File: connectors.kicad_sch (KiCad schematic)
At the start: 4 parts

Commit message: Schematic design complete
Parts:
- J1, J2: renamed from J?; footprint (none) -> Connector_PinHeader_2.54mm:PinHeader_1x04_P2.54mm_Vertical
- J3: renamed from J?; footprint (none) -> Connector_PinHeader_2.54mm:PinHeader_1x09_P2.54mm_Vertical
- J4: renamed from J?; footprint (none) -> Connector_PinHeader_2.54mm:PinHeader_2x03_P2.54mm_Vertical
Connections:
- net MISO: now reaches J4.1 (Pin_1)
- net Vcc: now reaches J4.2 (Pin_2)
- net Vcc: now also J1.2 (Pin_2), J2.2 (Pin_2), J3.9 (Pin_9)
- net SCK: now reaches J4.3 (Pin_3)
- net SCK: now also J1.4 (Pin_4)
- net MOSI: now reaches J4.4 (Pin_4)
- net RESET: now reaches J4.5 (Pin_5)
- net GND: now reaches J4.6 (Pin_6)
- net GND: now also J1.1 (Pin_1), J2.1 (Pin_1), J3.8 (Pin_8)
- net D2: now reaches J3.1 (Pin_1)
- net D3: now reaches J3.2 (Pin_2)
- net D4: now reaches J3.3 (Pin_3)
- net D5: now reaches J3.4 (Pin_4)
- net D6: now reaches J3.5 (Pin_5)
- net D7: now reaches J3.6 (Pin_6)
- net D8: now reaches J3.7 (Pin_7)
- net SDA: now reaches J1.3 (Pin_3)
- net RX: now reaches J2.3 (Pin_3)
- net TX: now reaches J2.4 (Pin_4)
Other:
- note added: "Connectors"
- title: (none) -> ${project_name}
- moved on the sheet: J1, J2, J3, J4
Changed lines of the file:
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@@
 (kicad_sch (version 20211123) (generator eeschema)
   (paper "A4")
-  (symbol (lib_id "Connector_Generic:Conn_02x03_Odd_Even") (at 222.25 112.395 0) (unit 1)
+  (title_block
+    (title "${project_name}")
+    (date "2022-08-29")
+    (rev "1")
+    (comment 1 "Project #2, KiCad Like a Pro Udemy course")
+    (comment 2 "MCU Datalogger with memory and clock")
+    (comment 3 "github.com/raghavmarwah")
+    (comment 4 "raghavmarwah.com")
+  )
+  (polyline (pts (xy 193.04 59.69) (xy 193.04 144.78))
+    (stroke (width 0) (type default) (color 0 0 0 0))
+  )
+  (polyline (pts (xy 92.075 59.69) (xy 92.075 60.325))
+    (stroke (width 0) (type default) (color 0 0 0 0))
+  )
+  (polyline (pts (xy 92.075 60.325) (xy 92.075 144.78))
+    (stroke (width 0) (type default) (color 0 0 0 0))
+  )
+  (polyline (pts (xy 92.075 144.78) (xy 193.04 144.78))
+    (stroke (width 0) (type default) (color 0 0 0 0))
+  )
+  (polyline (pts (xy 193.04 59.69) (xy 92.075 59.69))
+    (stroke (width 0) (type default) (color 0 0 0 0))
+  )
+  (text "Connectors" (at 92.075 59.69 0)
+    (effects (font (size 1.27 1.27)) (justify left bottom))
+  )
+  (hierarchical_label "Vcc" (shape passive) (at 125.095 81.915 0)
+    (effects (font (size 1.27 1.27)) (justify left))
+  )
+  (hierarchical_label "GND" (shape passive) (at 160.655 79.375 0)
+    (effects (font (size 1.27 1.27)) (justify left))
+  )
+  (hierarchical_label "D4" (shape bidirectional) (at 125.095 111.125 0)
+    (effects (font (size 1.27 1.27)) (justify left))
+  )
+  (hierarchical_label "Vcc" (shape passive) (at 160.655 81.915 0)
+    (effects (font (size 1.27 1.27)) (justify left))
+  )
+  (hierarchical_label "SCK" (shape passive) (at 125.095 86.995 0)
+    (effects (font (size 1.27 1.27)) (justify left))
+  )
+  (hierarchical_label "SCK" (shape passive) (at 152.4 114.935 180)
+    (effects (font (size 1.27 1.27)) (justify right))
+  )
+  (hierarchical_label "D6" (shape bidirectional) (at 125.095 116.205 0)
+    (effects (font (size 1.27 1.27)) (justify left))
+  )
+  (hierarchical_label "GND" (shape passive) (at 165.1 117.475 0)
+    (effects (font (size 1.27 1.27)) (justify left))
+  )
+  (hierarchical_label "GND" (shape passive) (at 125.095 123.825 0)
+    (effects (font (size 1.27 1.27)) (justify left))
+  )
+  (hierarchical_label "D2" (shape bidirectional) (at 125.095 106.045 0)
+    (effects (font (size 1.27 1.27)) (justify left))
+  )
+  (hierarchical_label "TX" (shape output) (at 160.655 86.995 0)
+    (effects (font (size 1.27 1.27)) (justify left))
+  )
+  (hierarchical_label "SDA" (shape bidirectional) (at 125.095 84.455 0)
+    (effects (font (size 1.27 1.27)) (justify left))
+  )
+  (hierarchical_label "D3" (shape bidirectional) (at 125.095 108.585 0)
+    (effects (font (size 1.27 1.27)) (justify left))
+  )
+  (hierarchical_label "RESET" (shape passive) (at 152.4 117.475 180)
+    (effects (font (size 1.27 1.27)) (justify right))
+  )
+  (hierarchical_label "Vcc" (shape passive) (at 125.095 126.365 0)
+    (effects (font (size 1.27 1.27)) (justify left))
+  )
+  (hierarchical_label "D5" (shape bidirectional) (at 125.095 113.665 0)
+    (effects (font (size 1.27 1.27)) (justify left))
+  )
+  (hierarchical_label "D8" (shape bidirectional) (at 125.095 121.285 0)
+    (effects (font (size 1.27 1.27)) (justify left))
+  )
+  (hierarchical_label "MOSI" (shape input) (at 165.1 114.935 0)
+    (effects (font (size 1.27 1.27)) (justify left))
+  )
+  (hierarchical_label "D7" (shape bidirectional) (at 125.095 118.745 0)
+    (effects (font (size 1.27 1.27)) (justify left))
+  )
+  (hierarchical_label "RX" (shape input) (at 160.655 84.455 0)
+    (effects (font (size 1.27 1.27)) (justify left))
+  )
+  (hierarchical_label "Vcc" (shape passive) (at 165.1 112.395 0)
+    (effects (font (size 1.27 1.27)) (justify left))
+  )
+  (hierarchical_label "MISO" (shape output) (at 152.4 112.395 180)
+    (effects (font (size 1.27 1.27)) (justify right))
+  )
+  (hierarchical_label "GND" (shape passive) (at 125.095 79.375 0)
+    (effects (font (size 1.27 1.27)) (justify left))
+  )
+  (symbol (lib_id "Connector_Generic:Conn_02x03_Odd_Even") (at 157.48 114.935 0) (unit 1)
     (in_bom yes) (on_board yes) (fields_autoplaced)
-    (property "Reference" "J?" (id 0) (at 223.52 102.87 0))
-    (property "Value" "Conn_02x03_Odd_Even" (id 1) (at 223.52 105.41 0))
-    (property "Footprint" "" (id 2) (at 222.25 112.395 0)
+    (property "Reference" "J4" (id 0) (at 158.75 105.41 0))
+    (property "Value" "Conn_02x03_Odd_Even" (id 1) (at 158.75 107.95 0))
+    (property "Footprint" "Connector_PinHeader_2.54mm:PinHeader_2x03_P2.54mm_Vertical" (id 2) (at 157.48 114.935 0)
       (effects (font (size 1.27 1.27)) hide)
     )
-    (property "Datasheet" "~" (id 3) (at 222.25 112.395 0)
+    (property "Datasheet" "~" (id 3) (at 157.48 114.935 0)
       (effects (font (size 1.27 1.27)) hide)
     )
@@
     (pin "6")
   )
-  (symbol (lib_id "Connector:Conn_01x09_Male") (at 182.88 102.235 0) (unit 1)
+  (symbol (lib_id "Connector:Conn_01x09_Male") (at 120.015 116.205 0) (unit 1)
     (in_bom yes) (on_board yes)
-    (property "Reference" "J?" (id 0) (at 183.515 86.36 0))
-    (property "Value" "Conn_01x09_Male" (id 1) (at 183.515 88.9 0))
-    (property "Footprint" "" (id 2) (at 182.88 102.235 0)
+    (property "Reference" "J3" (id 0) (at 120.65 100.33 0))
+    (property "Value" "Conn_01x09_Male" (id 1) (at 120.65 102.87 0))
+    (property "Footprint" "Connector_PinHeader_2.54mm:PinHeader_1x09_P2.54mm_Vertical" (id 2) (at 120.015 116.205 0)
       (effects (font (size 1.27 1.27)) hide)
     )
-    (property "Datasheet" "~" (id 3) (at 182.88 102.235 0)
+    (property "Datasheet" "~" (id 3) (at 120.015 116.205 0)
       (effects (font (size 1.27 1.27)) hide)
     )
-    (property "Purpose" "GPIO" (id 4) (at 186.055 114.3 0))
+    (property "Purpose" "GPIO" (id 4) (at 123.19 128.27 0))
     (pin "1")
     (pin "2")
@@
     (pin "9")
   )
-  (symbol (lib_id "Connector:Conn_01x04_Male") (at 157.48 86.36 0) (unit 1)
+  (symbol (lib_id "Connector:Conn_01x04_Male") (at 120.015 81.915 0) (unit 1)
     (in_bom yes) (on_board yes)
-    (property "Reference" "J?" (id 0) (at 158.115 78.74 0))
-    (property "Value" "Conn_01x04_Male" (id 1) (at 158.115 81.28 0))
-    (property "Footprint" "" (id 2) (at 157.48 86.36 0)
+    (property "Reference" "J1" (id 0) (at 120.65 74.295 0))
+    (property "Value" "Conn_01x04_Male" (id 1) (at 120.65 76.835 0))
+    (property "Footprint" "Connector_PinHeader_2.54mm:PinHeader_1x04_P2.54mm_Vertical" (id 2) (at 120.015 81.915 0)
       (effects (font (size 1.27 1.27)) hide)
     )
-    (property "Datasheet" "~" (id 3) (at 157.48 86.36 0)
+    (property "Datasheet" "~" (id 3) (at 120.015 81.915 0)
       (effects (font (size 1.27 1.27)) hide)
     )
-    (property "Purpose" "I2C" (id 4) (at 160.02 93.345 0))
+    (property "Purpose" "I2C" (id 4) (at 122.555 88.9 0))
     (pin "1")
     (pin "2")
@@
     (pin "4")
   )
-  (symbol (lib_id "Connector:Conn_01x04_Male") (at 158.75 107.95 0) (unit 1)
+  (symbol (lib_id "Connector:Conn_01x04_Male") (at 155.575 81.915 0) (unit 1)
     (in_bom yes) (on_board yes)
-    (property "Reference" "J?" (id 0) (at 159.385 100.33 0))
-    (property "Value" "Conn_01x04_Male" (id 1) (at 159.385 102.87 0))
-    (property "Footprint" "" (id 2) (at 158.75 107.95 0)
+    (property "Reference" "J2" (id 0) (at 156.21 74.295 0))
+    (property "Value" "Conn_01x04_Male" (id 1) (at 156.21 76.835 0))
+    (property "Footprint" "Connector_PinHeader_2.54mm:PinHeader_1x04_P2.54mm_Vertical" (id 2) (at 155.575 81.915 0)
       (effects (font (size 1.27 1.27)) hide)
     )
-    (property "Datasheet" "~" (id 3) (at 158.75 107.95 0)
+    (property "Datasheet" "~" (id 3) (at 155.575 81.915 0)
       (effects (font (size 1.27 1.27)) hide)
     )
-    (property "Purpose" "Serial UART" (id 4) (at 161.29 114.935 0))
+    (property "Purpose" "Serial UART" (id 4) (at 158.115 88.9 0))
     (pin "1")
     (pin "2")

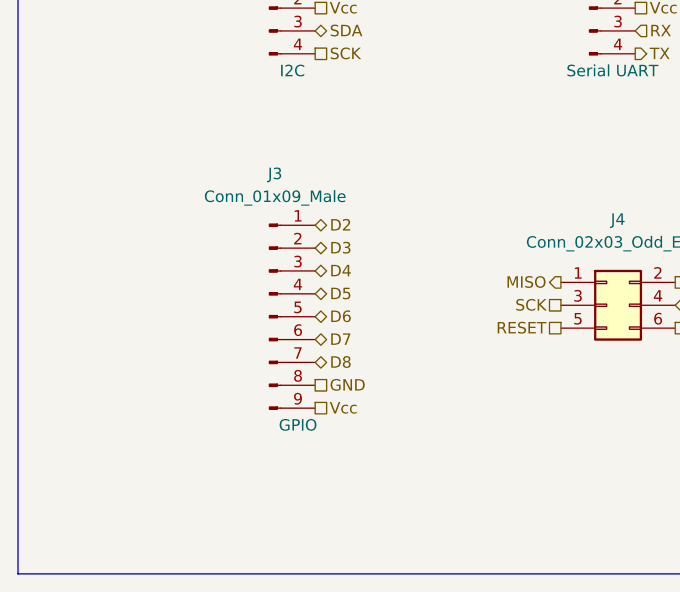
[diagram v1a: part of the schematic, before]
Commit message: Minor changes to PCB footprints
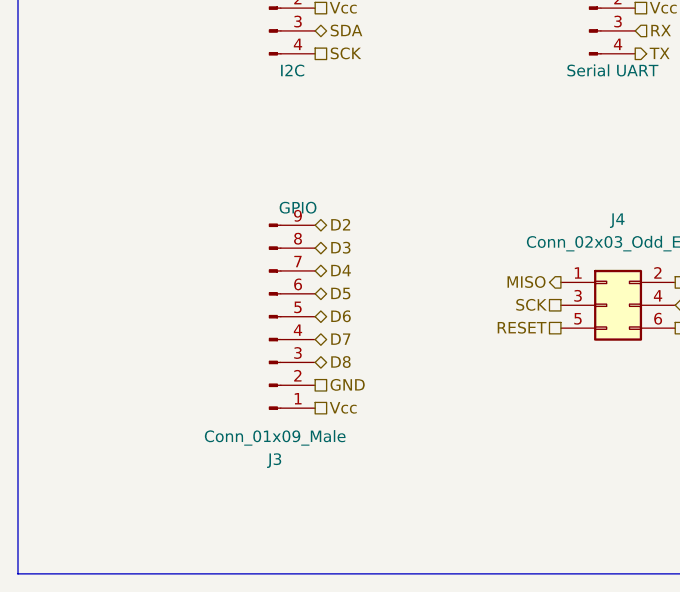
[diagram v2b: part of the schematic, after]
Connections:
- net D2: now also J3.9 (Pin_9); no longer J3.1 (Pin_1)
- net D3: now also J3.8 (Pin_8); no longer J3.2 (Pin_2)
- net D4: now also J3.7 (Pin_7); no longer J3.3 (Pin_3)
- net D5: now also J3.6 (Pin_6); no longer J3.4 (Pin_4)
- net D7: now also J3.4 (Pin_4); no longer J3.6 (Pin_6)
- net D8: now also J3.3 (Pin_3); no longer J3.7 (Pin_7)
- net GND: now also J3.2 (Pin_2); no longer J3.8 (Pin_8)
- net Vcc: now also J3.1 (Pin_1); no longer J3.9 (Pin_9)
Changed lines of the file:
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@@
     (pin "6")
   )
-  (symbol (lib_id "Connector:Conn_01x09_Male") (at 120.015 116.205 0) (unit 1)
+  (symbol (lib_id "Connector:Conn_01x09_Male") (at 120.015 116.205 0) (mirror x) (unit 1)
     (in_bom yes) (on_board yes)
-    (property "Reference" "J3" (id 0) (at 120.65 100.33 0))
-    (property "Value" "Conn_01x09_Male" (id 1) (at 120.65 102.87 0))
+    (property "Reference" "J3" (id 0) (at 120.65 132.08 0))
+    (property "Value" "Conn_01x09_Male" (id 1) (at 120.65 129.54 0))
     (property "Footprint" "Connector_PinHeader_2.54mm:PinHeader_1x09_P2.54mm_Vertical" (id 2) (at 120.015 116.205 0)
       (effects (font (size 1.27 1.27)) hide)
@@
       (effects (font (size 1.27 1.27)) hide)
     )
-    (property "Purpose" "GPIO" (id 4) (at 123.19 128.27 0))
+    (property "Purpose" "GPIO" (id 4) (at 123.19 104.14 0))
     (pin "1")
     (pin "2")

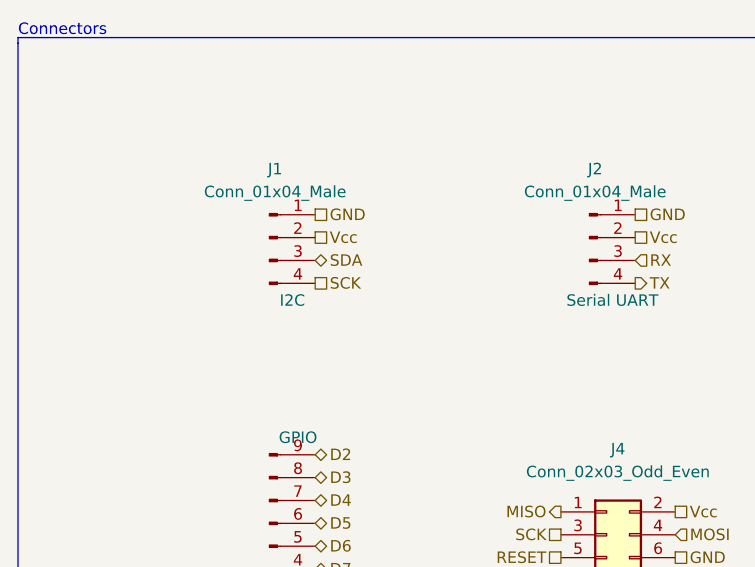
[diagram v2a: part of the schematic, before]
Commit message: Added SCL net to schematic and fixed errors
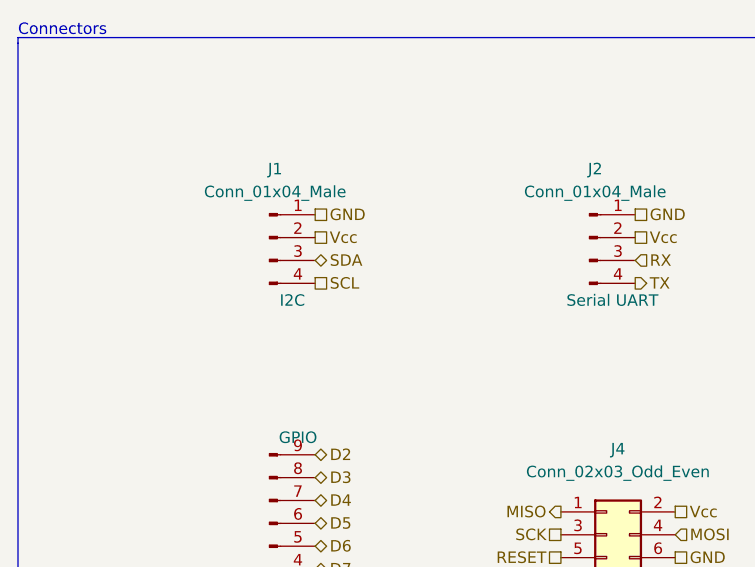
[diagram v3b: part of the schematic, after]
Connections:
- net SCK: no longer J1.4 (Pin_4)
- new net SCL: J1.4 (Pin_4)
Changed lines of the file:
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@@
     (effects (font (size 1.27 1.27)) (justify left))
   )
-  (hierarchical_label "SCK" (shape passive) (at 125.095 86.995 0)
+  (hierarchical_label "SCL" (shape passive) (at 125.095 86.995 0)
     (effects (font (size 1.27 1.27)) (justify left))
   )
